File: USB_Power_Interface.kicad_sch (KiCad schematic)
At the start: 33 parts, among them CN1 GT-USB-7014D, U1 TPS2121, U2 TPSM82903

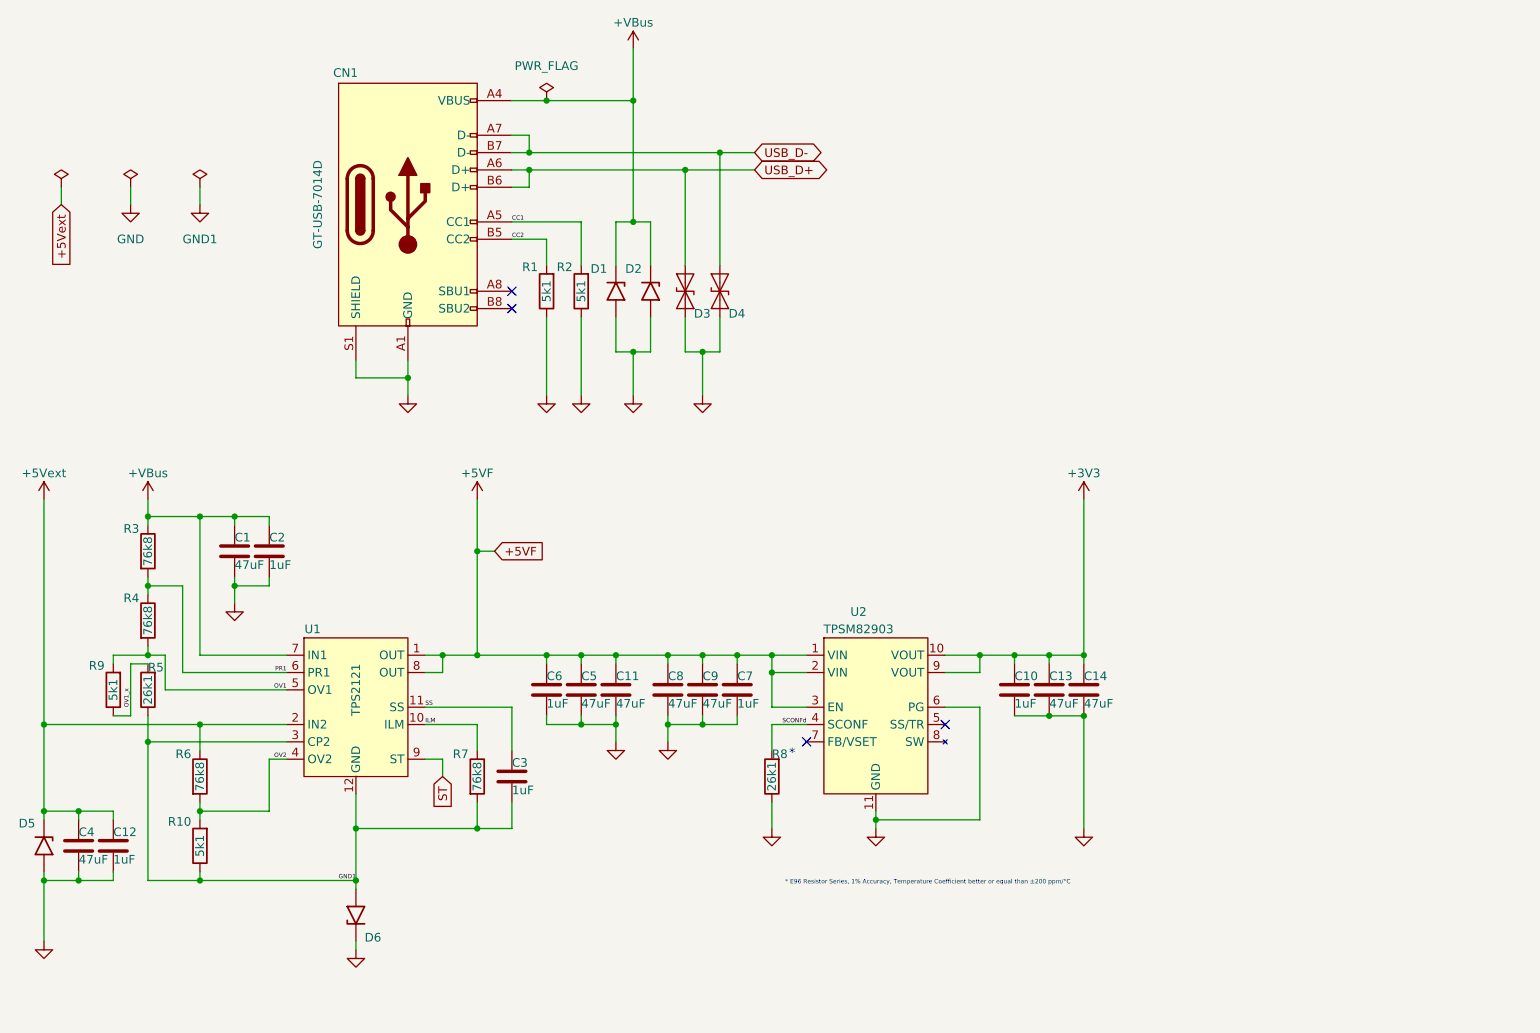
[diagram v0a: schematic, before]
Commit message: Update .gitignore, BOM-ESP32-S3 Pico D1.csv, CANBus_Interface.kicad_sch, and 14 more files
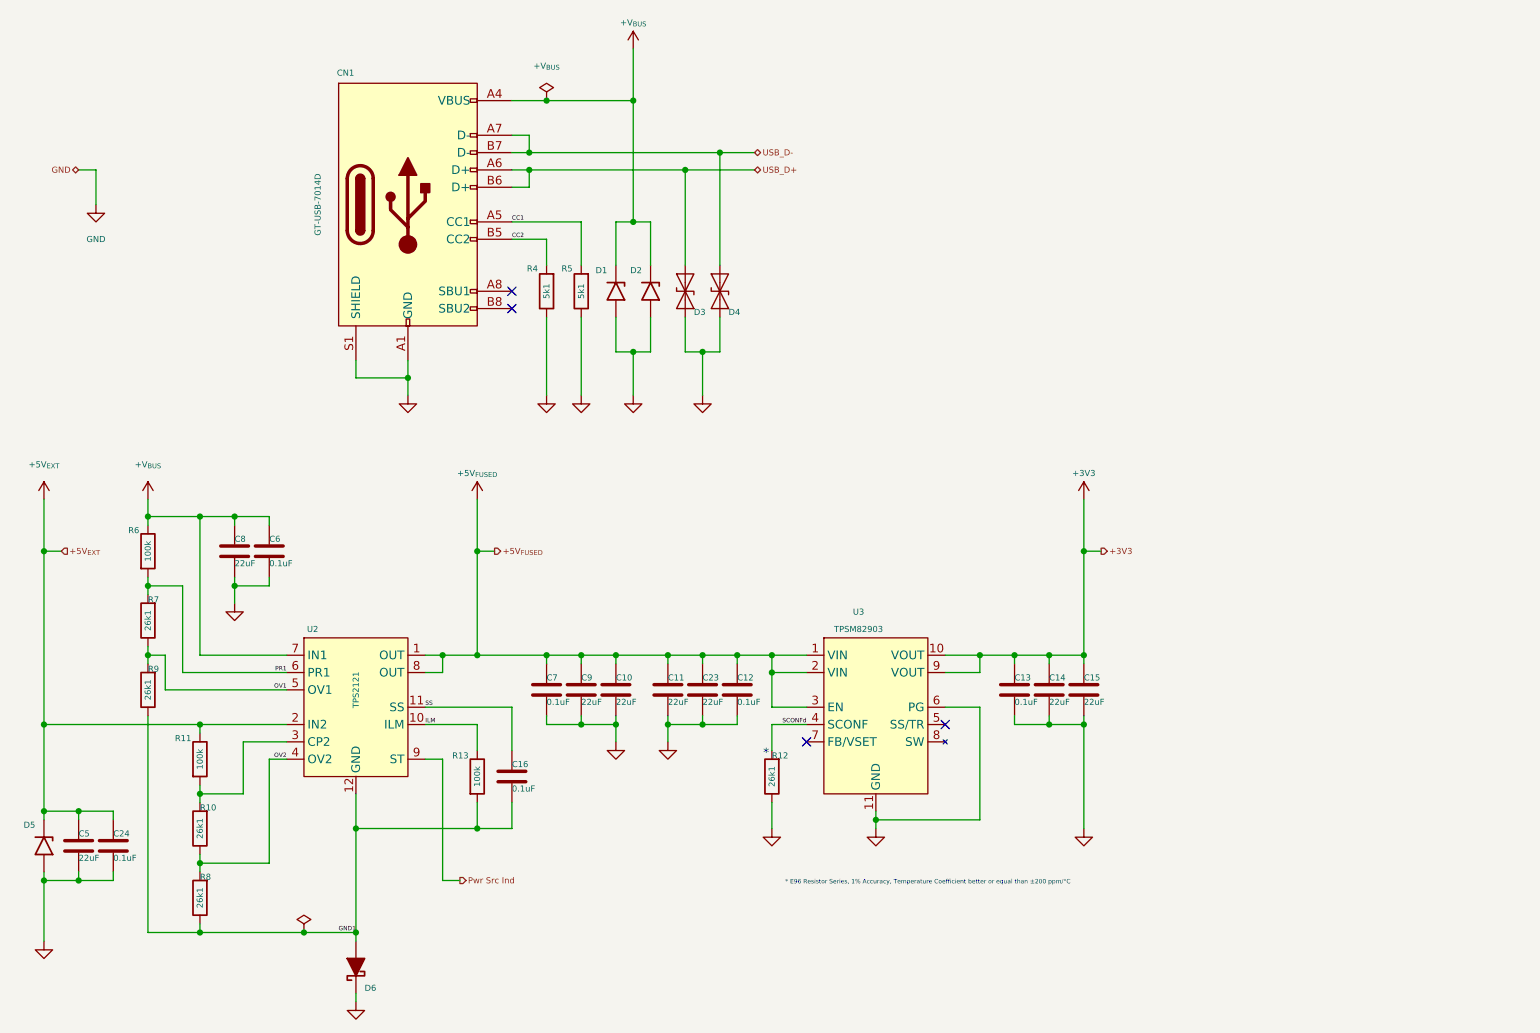
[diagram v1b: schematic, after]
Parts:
- removed C1, C4: 47uF, Capacitors:C_0603_Dense, symbol Device:C
- removed C2, C3: 1uF, Capacitors:C_0201_Dense, symbol Device:C
- removed R2, R9: 5k1, Resistors:R_0201_Dense, symbol Device:R
- removed R4, R6: 76k8, Resistors:R_0201_Dense, symbol Device:R
- added C15, C23: 22uF, Capacitors:C_0603_Dense, symbol Device:C
- added C16, C24: 0.1uF, Capacitors:C_0201_Dense, symbol Device:C
- added R11, R13: 100k, Resistors:R_0201_Dense, symbol Device:R
- added R12: 26k1, Resistors:R_0201_Dense, symbol Device:R
- added R5: 5k1, Resistors:R_0201_Dense, symbol Device:R
- C10: value 1uF -> 22uF; footprint Capacitors:C_0201_Dense -> Capacitors:C_0603_Dense; Distributor Link 1 https://www.digikey.com/en/products/detail/samsung-electro-mechanics/CL03A105MO3NRNH/5961282 -> https://www.digikey.com/en/products/detail/samsung-electro-mechanics/CL10A226MO7JZNC/7320581; Distributor Link 2 https://www.mouser.com/ProductDetail/Samsung-Electro-Mechanics/CL03A105MO3NRNH?qs=%252B6g0mu59x7LEwOOdfYkIjw%3D%3D -> https://www.mouser.com/ProductDetail/Samsung-Electro-Mechanics/CL10A226MO7JZNC?qs=sGAEpiMZZMvsSlwiRhF8qtsGU%2FCnaNeQBzruVQvBjN%2FZ5r%2FMGD9SXg%3D%3D; LCSC C307385 -> C2762594; Manufacturer Part Number CL03A105MO3NRNH -> CL10A226MO7JZNC
- C11, C14, C5, C8, C9: value 47uF -> 22uF; Distributor Link 1 https://www.digikey.com/en/products/detail/murata-electroni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 -> https://www.digikey.com/en/products/detail/samsung-electro-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; Distributor Link 2 https://www.mouser.com/ProductDetail/Murata-Electronics/GRM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 -> https://www.mouser.com/ProductDetail/Samsung-Electro-Mechan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; LCSC C140782 -> C2762594; Manufacturer Murata Electronics -> Samsung Electro-Mechanics; Manufacturer Part Number GRM188R60J476ME15D -> CL10A226MO7JZNC
- C12, C6, C7: value 1uF -> 0.1uF; Distributor Link 1 https://www.digikey.com/en/products/detail/samsung-electro-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 -> https://www.digikey.com/en/products/detail/murata-electroni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; Distributor Link 2 https://www.mouser.com/ProductDetail/Samsung-Electro-Mechan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 -> https://www.mouser.com/ProductDetail/Murata-Electronics/GRT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; LCSC C307385 -> C915760; Manufacturer Samsung Electro-Mechanics -> Murata Electronics; Manufacturer Part Number CL03A105MO3NRNH -> GRT033R61E104KE01D
- C13: value 47uF -> 0.1uF; footprint Capacitors:C_0603_Dense -> Capacitors:C_0201_Dense; Distributor Link 1 https://www.digikey.com/en/products/detail/murata-electronics/GRM188R60J476ME15D/5877410 -> https://www.digikey.com/en/products/detail/murata-electronics/GRT033R61E104KE01D/10696558; Distributor Link 2 https://www.mouser.com/ProductDetail/Murata-Electronics/GRM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 -> https://www.mouser.com/ProductDetail/Murata-Electronics/GRT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; LCSC C140782 -> C915760; Manufacturer Part Number GRM188R60J476ME15D -> GRT033R61E104KE01D
- D6: value D15V0H1U2LP-7B -> SDM1100LP-7; footprint Personal_FootprintLibrary:DFN1006-2 -> Personal_FootprintLibrary:DFN2020-2; symbol PersonalSchematicSymbolLibrary:TVS_Unidirectional -> PersonalSchematicSymbolLibrary:D_Schottky_Filled; Distributor Link 1 https://www.digikey.com/en/products/detail/diodes-incorporated/D15V0H1U2LP-7B/9089765 -> https://www.digikey.com/en/products/detail/diodes-incorporated/SDM1100LP-7/6010159; Distributor Link 2 https://www.mouser.com/ProductDetail/Diodes-Incorporated/D1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 -> https://www.mouser.com/ProductDetail/Diodes-Incorporated/SD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; LCSC C1973850 -> C6999905; Manufacturer Part Number D15V0H1U2LP-7B -> SDM1100LP-7
- R10: value 5k1 -> 26k1; Distributor Link 1 (none) -> https://www.digikey.com/en/products/detail/yageo/AC0201FR-0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; Distributor Link 2 https://www.mouser.com/ProductDetail/Royalohm/0201WMF5101TE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 -> https://www.mouser.com/ProductDetail/YAGEO/AC0201FR-0726K1L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; LCSC C270344 -> C910625; Manufacturer UNI-ROYAL(Uniroyal Elec) -> YAGEO; Manufacturer Part Number 0201WMF5101TEE -> AC0201FR-0726K1L
- R4: renamed from R1; Distributor Link 1 (none) -> https://www.digikey.com/en/products/detail/yageo/AC0201FR-0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; Distributor Link 2 https://www.mouser.com/ProductDetail/Royalohm/0201WMF5101TE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 -> https://www.mouser.com/ProductDetail/YAGEO/AC0201FR-075K1L?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; LCSC C270344 -> C226588; Manufacturer UNI-ROYAL(Uniroyal Elec) -> YAGEO; Manufacturer Part Number 0201WMF5101TEE -> AC0201FR-075K1L
- R6: renamed from R3; value 76k8 -> 100k; Distributor Link 1 https://www.digikey.com/en/products/detail/yageo/AC0201FR-0776K8L/5894812 -> https://www.digikey.com/en/products/detail/yageo/AC0201FR-07100KL/5894217; Distributor Link 2 https://www.mouser.com/ProductDetail/YAGEO/AC0201FR-0776K8L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 -> https://www.mouser.com/ProductDetail/YAGEO/AC0201FR-07100KL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; LCSC C850692 -> C226394; Manufacturer Part Number AC0201FR-0776K8L -> AC0201FR-07100KL
- R7: value 76k8 -> 26k1; Distributor Link 1 https://www.digikey.com/en/products/detail/yageo/AC0201FR-0776K8L/5894812 -> https://www.digikey.com/en/products/detail/yageo/AC0201FR-0726K1L/5894466; Distributor Link 2 https://www.mouser.com/ProductDetail/YAGEO/AC0201FR-0776K8L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 -> https://www.mouser.com/ProductDetail/YAGEO/AC0201FR-0726K1L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; LCSC C850692 -> C910625; Manufacturer Part Number AC0201FR-0776K8L -> AC0201FR-0726K1L
- R8: Distributor Link 1 https://www.digikey.com/en/products/detail/yageo/RC0201DR-0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 -> https://www.digikey.com/en/products/detail/yageo/AC0201FR-0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; Distributor Link 2 https://www.mouser.com/ProductDetail/YAGEO/RC0201DR-0726K1L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 -> https://www.mouser.com/ProductDetail/YAGEO/AC0201FR-0726K1L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; LCSC C851693 -> C910625; Manufacturer Part Number RC0201DR-0726K1L -> AC0201FR-0726K1L
- R9: renamed from R5; Distributor Link 1 https://www.digikey.com/en/products/detail/yageo/RC0201DR-0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 -> https://www.digikey.com/en/products/detail/yageo/AC0201FR-0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; Distributor Link 2 https://www.mouser.com/ProductDetail/YAGEO/RC0201DR-0726K1L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 -> https://www.mouser.com/ProductDetail/YAGEO/AC0201FR-0726K1L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; LCSC C851693 -> C910625; Manufacturer Part Number RC0201DR-0726K1L -> AC0201FR-0726K1L
- U2: renamed from U1; symbol PersonalSchematicSymbolLibrary:TPS2121 -> My Power Management:TPS2121
- U3: renamed from U2; symbol PersonalSchematicSymbolLibrary:TPSM82903 -> My Power DCDC:TPSM8290x
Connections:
- net OV1_x is gone; now on net OV1: R9.2
- net +3V3: now also C15.1; no longer C10.1
- net CC1: now also R5.2
- net GND: now also C15.2, C23.2, C24.2, R12.1, R5.1; no longer R8.1
- net GND1: now also R8.1, C16.2, R13.2; no longer R10.1, R7.2, U2.3 (CP2)
- net ILM: now also R13.1; no longer R7.1
- net OV1: now also R7.1
- net OV2: now also R10.1, R8.2; no longer R10.2
- net PR1: now also R7.2
- net SCONFd: now also R12.2; no longer R8.2
- net SS: now also C16.1
- net +5VF renamed +5V_{FUSED}
- net +5V_{FUSED}: now also C10.1, C12.1, C23.1; no longer C5.1, C6.1, C8.1
- net +5Vext renamed +5V_{EXT}
- net +5V_{EXT}: now also C5.1, C24.1, R11.1; no longer C12.1
- net +VBus renamed +V_{BUS}
- net +V_{BUS}: now also C6.1, C8.1
- net ST renamed Pwr Src Ind
- new net: R10.2, R11.2, U2.3 (CP2)

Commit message: Update CANBus_Interface.kicad_sch, ESP32-S3 D1 Pico Board.kicad_sch, ESP32-S3 Pico D1.kicad_pcb, and 15 more files
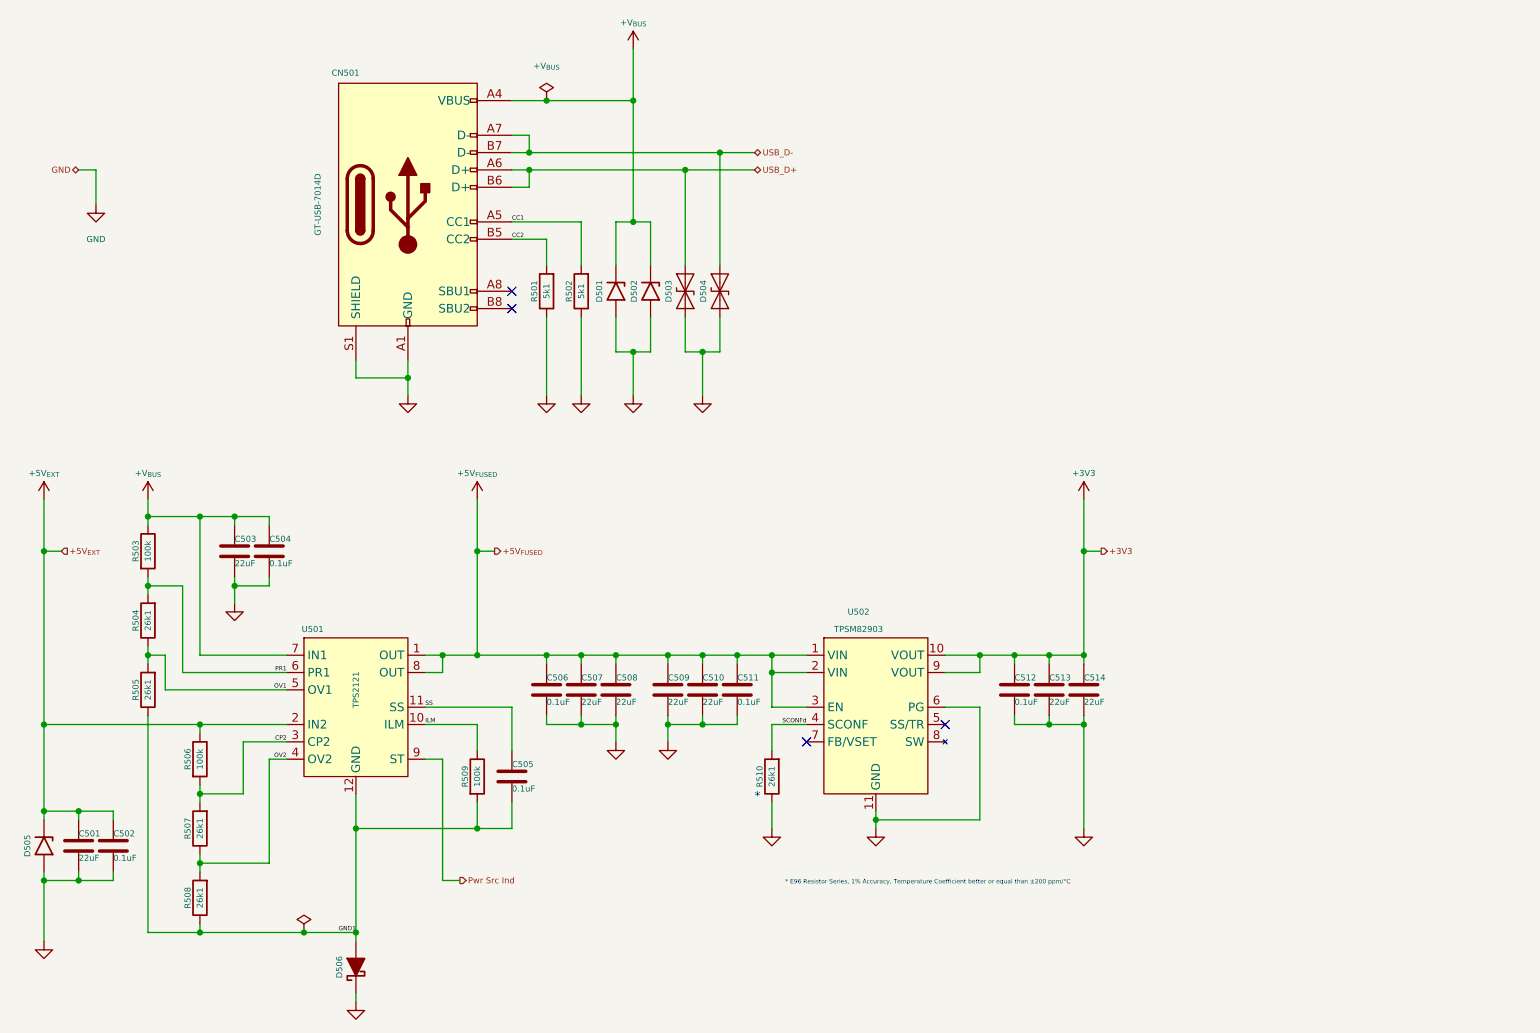
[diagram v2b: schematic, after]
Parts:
- C501: renamed from C5; footprint Capacitors:C_0603_Dense -> My Capacitors:C_0603_Dense; Distributor Link 1 https://www.digikey.com/en/products/detail/samsung-electro-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 -> https://www.digikey.com/en/products/detail/murata-electroni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; Distributor Link 2 https://www.mouser.com/ProductDetail/Samsung-Electro-Mechan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 -> https://www.mouser.com/ProductDetail/Murata-Electronics/GRM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; LCSC C2762594 -> C29519229; Manufacturer Samsung Electro-Mechanics -> Murata Electronics; Manufacturer Part Number CL10A226MO7JZNC -> GRM188C61E226ME01D
- C502: renamed from C24; footprint Capacitors:C_0201_Dense -> My Capacitors:C_0201_Dense
- C503: renamed from C8; footprint Capacitors:C_0603_Dense -> My Capacitors:C_0603_Dense; Distributor Link 1 https://www.digikey.com/en/products/detail/samsung-electro-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 -> https://www.digikey.com/en/products/detail/murata-electroni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; Distributor Link 2 https://www.mouser.com/ProductDetail/Samsung-Electro-Mechan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 -> https://www.mouser.com/ProductDetail/Murata-Electronics/GRM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; LCSC C2762594 -> C29519229; Manufacturer Samsung Electro-Mechanics -> Murata Electronics; Manufacturer Part Number CL10A226MO7JZNC -> GRM188C61E226ME01D
- C504: renamed from C6; footprint Capacitors:C_0201_Dense -> My Capacitors:C_0201_Dense
- C505: renamed from C16; footprint Capacitors:C_0201_Dense -> My Capacitors:C_0201_Dense
- C506: renamed from C7; footprint Capacitors:C_0201_Dense -> My Capacitors:C_0201_Dense
- C507: renamed from C9; footprint Capacitors:C_0603_Dense -> My Capacitors:C_0603_Dense; Distributor Link 1 https://www.digikey.com/en/products/detail/samsung-electro-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 -> https://www.digikey.com/en/products/detail/murata-electroni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; Distributor Link 2 https://www.mouser.com/ProductDetail/Samsung-Electro-Mechan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 -> https://www.mouser.com/ProductDetail/Murata-Electronics/GRM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; LCSC C2762594 -> C29519229; Manufacturer Samsung Electro-Mechanics -> Murata Electronics; Manufacturer Part Number CL10A226MO7JZNC -> GRM188C61E226ME01D
- C508: renamed from C10; footprint Capacitors:C_0603_Dense -> My Capacitors:C_0603_Dense; Distributor Link 1 https://www.digikey.com/en/products/detail/samsung-electro-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 -> https://www.digikey.com/en/products/detail/murata-electroni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; Distributor Link 2 https://www.mouser.com/ProductDetail/Samsung-Electro-Mechan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 -> https://www.mouser.com/ProductDetail/Murata-Electronics/GRM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; LCSC C2762594 -> C29519229; Manufacturer Samsung Electro-Mechanics -> Murata Electronics; Manufacturer Part Number CL10A226MO7JZNC -> GRM188C61E226ME01D
- C509: renamed from C11; footprint Capacitors:C_0603_Dense -> My Capacitors:C_0603_Dense; Distributor Link 1 https://www.digikey.com/en/products/detail/samsung-electro-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 -> https://www.digikey.com/en/products/detail/murata-electroni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; Distributor Link 2 https://www.mouser.com/ProductDetail/Samsung-Electro-Mechan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 -> https://www.mouser.com/ProductDetail/Murata-Electronics/GRM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; LCSC C2762594 -> C29519229; Manufacturer Samsung Electro-Mechanics -> Murata Electronics; Manufacturer Part Number CL10A226MO7JZNC -> GRM188C61E226ME01D
- C510: renamed from C23; footprint Capacitors:C_0603_Dense -> My Capacitors:C_0603_Dense; Distributor Link 1 https://www.digikey.com/en/products/detail/samsung-electro-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 -> https://www.digikey.com/en/products/detail/murata-electroni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; Distributor Link 2 https://www.mouser.com/ProductDetail/Samsung-Electro-Mechan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 -> https://www.mouser.com/ProductDetail/Murata-Electronics/GRM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; LCSC C2762594 -> C29519229; Manufacturer Samsung Electro-Mechanics -> Murata Electronics; Manufacturer Part Number CL10A226MO7JZNC -> GRM188C61E226ME01D
- C511: renamed from C12; footprint Capacitors:C_0201_Dense -> My Capacitors:C_0201_Dense
- C512: renamed from C13; footprint Capacitors:C_0201_Dense -> My Capacitors:C_0201_Dense
- C513: renamed from C14; footprint Capacitors:C_0603_Dense -> My Capacitors:C_0603_Dense; Distributor Link 1 https://www.digikey.com/en/products/detail/samsung-electro-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 -> https://www.digikey.com/en/products/detail/murata-electroni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; Distributor Link 2 https://www.mouser.com/ProductDetail/Samsung-Electro-Mechan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 -> https://www.mouser.com/ProductDetail/Murata-Electronics/GRM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; LCSC C2762594 -> C29519229; Manufacturer Samsung Electro-Mechanics -> Murata Electronics; Manufacturer Part Number CL10A226MO7JZNC -> GRM188C61E226ME01D
- C514: renamed from C15; footprint Capacitors:C_0603_Dense -> My Capacitors:C_0603_Dense; Distributor Link 1 https://www.digikey.com/en/products/detail/samsung-electro-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 -> https://www.digikey.com/en/products/detail/murata-electroni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; Distributor Link 2 https://www.mouser.com/ProductDetail/Samsung-Electro-Mechan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 -> https://www.mouser.com/ProductDetail/Murata-Electronics/GRM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; LCSC C2762594 -> C29519229; Manufacturer Samsung Electro-Mechanics -> Murata Electronics; Manufacturer Part Number CL10A226MO7JZNC -> GRM188C61E226ME01D
- D506: renamed from D6; value SDM1100LP-7 -> PMEG4002ESFYL; footprint Personal_FootprintLibrary:DFN2020-2 -> Personal_FootprintLibrary:DSN0603-2; Distributor Link 1 https://www.digikey.com/en/products/detail/diodes-incorpora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 -> https://www.digikey.com/en/products/detail/nexperia-usa-inc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; Distributor Link 2 https://www.mouser.com/ProductDetail/Diodes-Incorporated/SD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 -> https://www.mouser.com/ProductDetail/Nexperia/PMEG4002ESFYL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; LCSC C6999905 -> C22435168; Manufacturer Diodes Incorporated -> Nexperia USA Inc.; Manufacturer Part Number SDM1100LP-7 -> PMEG4002ESFYL
- R501: renamed from R4; footprint Resistors:R_0201_Dense -> My Resistors:R_0201_Dense
- R502: renamed from R5; footprint Resistors:R_0201_Dense -> My Resistors:R_0201_Dense
- R503: renamed from R6; footprint Resistors:R_0201_Dense -> My Resistors:R_0201_Dense
- R504: renamed from R7; footprint Resistors:R_0201_Dense -> My Resistors:R_0201_Dense
- R505: renamed from R9; footprint Resistors:R_0201_Dense -> My Resistors:R_0201_Dense
- R506: renamed from R11; footprint Resistors:R_0201_Dense -> My Resistors:R_0201_Dense
- R507: renamed from R10; footprint Resistors:R_0201_Dense -> My Resistors:R_0201_Dense
- R508: renamed from R8; footprint Resistors:R_0201_Dense -> My Resistors:R_0201_Dense
- R509: renamed from R13; footprint Resistors:R_0201_Dense -> My Resistors:R_0201_Dense
- R510: renamed from R12; footprint Resistors:R_0201_Dense -> My Resistors:R_0201_Dense
- renumbered CN1 to CN501, D1 to D501, D2 to D502, D3 to D503, D4 to D504, D5 to D505, U2 to U501, U3 to U502
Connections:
- net CP2: now reaches R506.2, R507.2, U501.3 (CP2)
